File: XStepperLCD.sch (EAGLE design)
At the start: 40 parts, among them Q1 CSTCR6M00G53Z, U1 LCD-16X2NOHOLES, X1 RJ45-6L-B

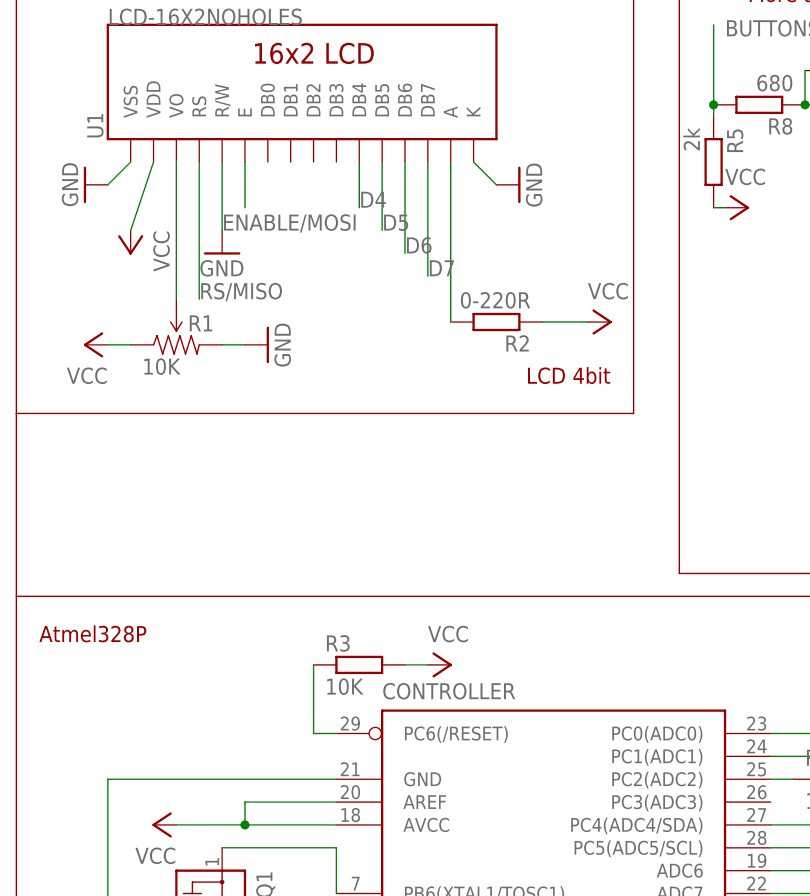
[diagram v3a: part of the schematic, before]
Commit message: finish to produce
Route new and set some via's.
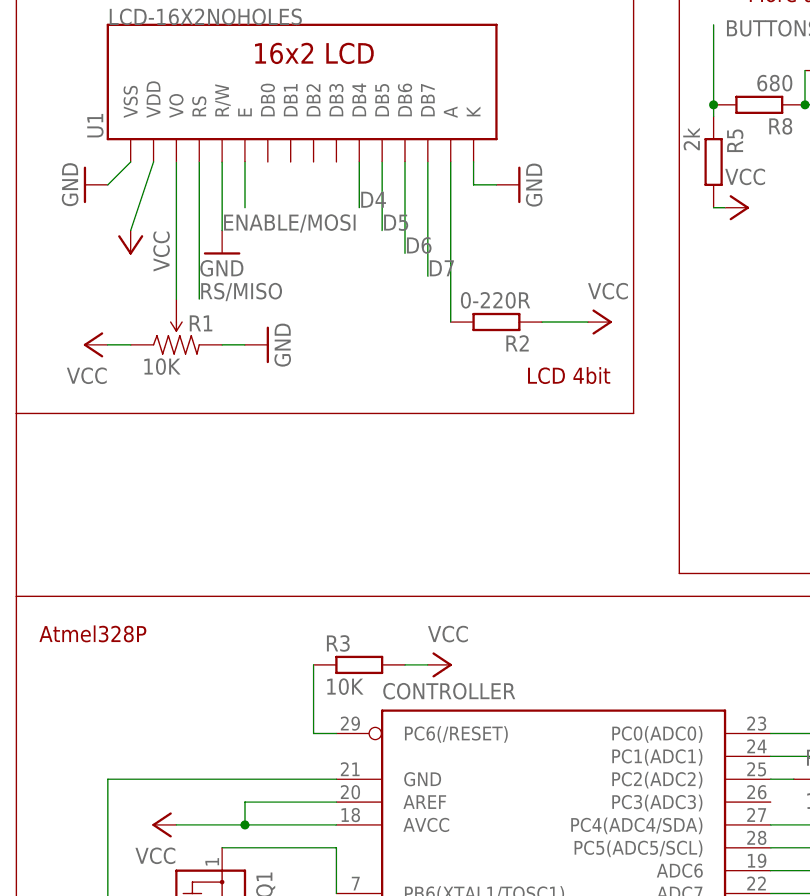
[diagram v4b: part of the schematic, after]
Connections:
- new net N$16: 328P.PC6(/RESET), R3.1
- net RESET: no longer 328P.PC6(/RESET), R3.1
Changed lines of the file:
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@@
 <?xml version="1.0" encoding="utf-8"?>
 <!DOCTYPE eagle SYSTEM "eagle.dtd">
-<eagle version="6.3">
+<eagle version="7.1.0">
 <drawing>
 <settings>
@@
 <pinref part="GND7" gate="1" pin="GND"/>
 <pinref part="U1" gate="G$1" pin="VSS"/>
-<wire x1="48.26" y1="86.36" x2="50.8" y2="83.82" width="0.1524" layer="91"/>
-<pinref part="GND1" gate="1" pin="GND"/>
-<pinref part="U1" gate="G$1" pin="K"/>
 </segment>
 <segment>
@@
 <junction x="162.56" y="-7.62"/>
 </segment>
+<segment>
+<pinref part="GND1" gate="1" pin="GND"/>
+<pinref part="U1" gate="G$1" pin="K"/>
+<wire x1="50.8" y1="83.82" x2="48.26" y2="83.82" width="0.1524" layer="91"/>
+<wire x1="48.26" y1="83.82" x2="48.26" y2="86.36" width="0.1524" layer="91"/>
+</segment>
 </net>
 <net name="TX" class="0">
@@
 </net>
 <net name="RESET" class="0">
-<segment>
-<pinref part="328P" gate="G$1" pin="PC6(/RESET)"/>
-<wire x1="30.48" y1="22.86" x2="33.02" y2="22.86" width="0.1524" layer="91"/>
-<wire x1="30.48" y1="22.86" x2="30.48" y2="30.48" width="0.1524" layer="91"/>
-<pinref part="R3" gate="G$1" pin="1"/>
-</segment>
 <segment>
 <pinref part="C13" gate="G$1" pin="2"/>
@@
 </segment>
 </net>
+<net name="N$16" class="0">
+<segment>
+<pinref part="328P" gate="G$1" pin="PC6(/RESET)"/>
+<pinref part="R3" gate="G$1" pin="1"/>
+<wire x1="33.02" y1="22.86" x2="30.48" y2="22.86" width="0.1524" layer="91"/>
+<wire x1="30.48" y1="22.86" x2="30.48" y2="30.48" width="0.1524" layer="91"/>
+</segment>
+</net>
